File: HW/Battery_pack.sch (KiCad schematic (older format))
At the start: 10 parts

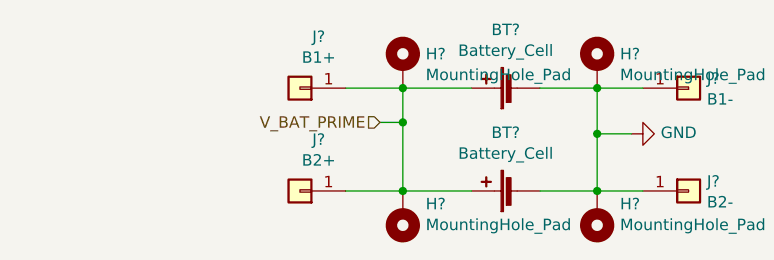
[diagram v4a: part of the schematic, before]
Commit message: add polyfuse for battery, remove resistor by SY8105, fix mistake by charger
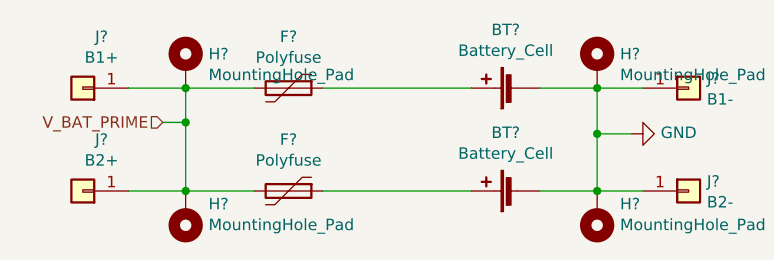
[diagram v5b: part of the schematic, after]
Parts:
- added F? (x2): Polyfuse, symbol Device:Polyfuse
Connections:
- net V_BAT_PRIME: now also F?.2, F?.2; no longer BT?.1 (+), BT?.1 (+)
- new net: BT?.1 (+), F?.1 (x2)
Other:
- moved on the sheet: H?, J?
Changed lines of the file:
@@
 $Descr A4 11693 8268
 encoding utf-8
-Sheet 8 42
+Sheet 13 42
 Title ""
 Date ""
@@
 L Connector_Generic:Conn_01x01 J?
 U 1 1 5F7477BC
-P 3950 3100
-F 0 "J?" H 3868 2875 50  0000 C CNN
-F 1 "B1+" H 3868 2966 50  0000 C CNN
-F 2 "" H 3950 3100 50  0001 C CNN
-F 3 "~" H 3950 3100 50  0001 C CNN
-	1    3950 3100
+P 3000 3100
+F 0 "J?" H 2918 2875 50  0000 C CNN
+F 1 "B1+" H 2918 2966 50  0000 C CNN
+F 2 "" H 3000 3100 50  0001 C CNN
+F 3 "~" H 3000 3100 50  0001 C CNN
+	1    3000 3100
 	-1   0    0    1
 $EndComp
@@
 L Connector_Generic:Conn_01x01 J?
 U 1 1 5F747F73
-P 3950 3550
-F 0 "J?" H 3868 3325 50  0000 C CNN
-F 1 "B2+" H 3868 3416 50  0000 C CNN
-F 2 "" H 3950 3550 50  0001 C CNN
-F 3 "~" H 3950 3550 50  0001 C CNN
-	1    3950 3550
+P 3000 3550
+F 0 "J?" H 2918 3325 50  0000 C CNN
+F 1 "B2+" H 2918 3416 50  0000 C CNN
+F 2 "" H 3000 3550 50  0001 C CNN
+F 3 "~" H 3000 3550 50  0001 C CNN
+	1    3000 3550
 	-1   0    0    1
 $EndComp
@@
 	5450 3100 5250 3100
 Wire Wire Line
-	4700 3100 4400 3100
+	3750 3100 3450 3100
 Wire Wire Line
-	4150 3550 4400 3550
+	3200 3550 3450 3550
 Wire Wire Line
 	5250 3100 5250 3300
@@
 	5250 3550 5000 3550
 Wire Wire Line
-	4400 3100 4400 3250
-Connection ~ 4400 3100
+	3450 3100 3450 3250
+Connection ~ 3450 3100
 Wire Wire Line
-	4400 3100 4150 3100
-Connection ~ 4400 3550
+	3450 3100 3200 3100
+Connection ~ 3450 3550
 Wire Wire Line
-	4400 3550 4700 3550
+	3450 3550 3750 3550
 $Comp
 L power:GND #PWR?
@@
 Wire Wire Line
 	5250 3300 5250 3550
-Text HLabel 4300 3250 0    50   Input ~ 0
+Text HLabel 3350 3250 0    50   Input ~ 0
 V_BAT_PRIME
 Wire Wire Line
-	4300 3250 4400 3250
-Connection ~ 4400 3250
+	3350 3250 3450 3250
+Connection ~ 3450 3250
 Wire Wire Line
-	4400 3250 4400 3550
+	3450 3250 3450 3550
 $Comp
 L Mechanical:MountingHole_Pad H?
 U 1 1 5F74F82F
-P 4400 3000
-F 0 "H?" H 4500 3049 50  0000 L CNN
-F 1 "MountingHole_Pad" H 4500 2958 50  0000 L CNN
-F 2 "" H 4400 3000 50  0001 C CNN
-F 3 "~" H 4400 3000 50  0001 C CNN
-	1    4400 3000
+P 3450 3000
+F 0 "H?" H 3550 3049 50  0000 L CNN
+F 1 "MountingHole_Pad" H 3550 2958 50  0000 L CNN
+F 2 "" H 3450 3000 50  0001 C CNN
+F 3 "~" H 3450 3000 50  0001 C CNN
+	1    3450 3000
 	1    0    0    -1
 $EndComp
@@
 L Mechanical:MountingHole_Pad H?
 U 1 1 5F7501BB
-P 4400 3650
-F 0 "H?" H 4300 3607 50  0000 R CNN
-F 1 "MountingHole_Pad" H 4300 3698 50  0000 R CNN
-F 2 "" H 4400 3650 50  0001 C CNN
-F 3 "~" H 4400 3650 50  0001 C CNN
-	1    4400 3650
+P 3450 3650
+F 0 "H?" H 3350 3607 50  0000 R CNN
+F 1 "MountingHole_Pad" H 3350 3698 50  0000 R CNN
+F 2 "" H 3450 3650 50  0001 C CNN
+F 3 "~" H 3450 3650 50  0001 C CNN
+	1    3450 3650
 	-1   0    0    1
 $EndComp
+$Comp
+L Device:Polyfuse F?
+U 1 1 5F77C417
+P 3900 3100
+F 0 "F?" V 3675 3100 50  0000 C CNN
+F 1 "Polyfuse" V 3766 3100 50  0000 C CNN
+F 2 "" H 3950 2900 50  0001 L CNN
+F 3 "~" H 3900 3100 50  0001 C CNN
+	1    3900 3100
+	0    1    1    0
+$EndComp
+$Comp
+L Device:Polyfuse F?
+U 1 1 5F77C5DC
+P 3900 3550
+F 0 "F?" V 3675 3550 50  0000 C CNN
+F 1 "Polyfuse" V 3766 3550 50  0000 C CNN
+F 2 "" H 3950 3350 50  0001 L CNN
+F 3 "~" H 3900 3550 50  0001 C CNN
+	1    3900 3550
+	0    1    1    0
+$EndComp
+Wire Wire Line
+	4050 3100 4700 3100
+Wire Wire Line
+	4050 3550 4700 3550
 $EndSCHEMATC

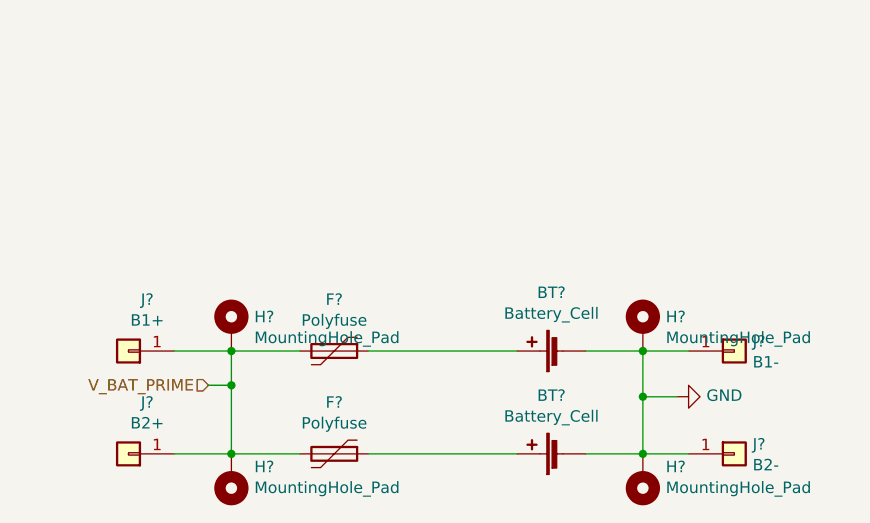
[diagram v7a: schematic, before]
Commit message: new battery pack schematic
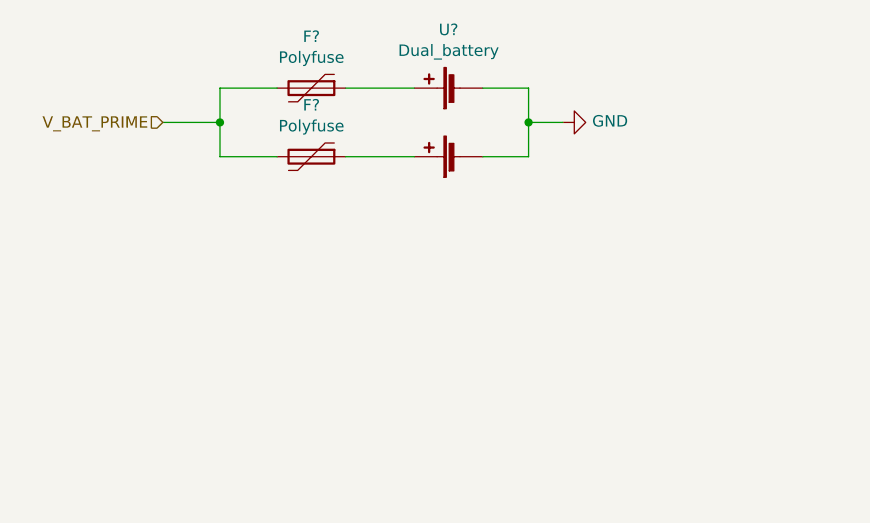
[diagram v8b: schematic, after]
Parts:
- removed BT? (x2): Battery_Cell, symbol Device:Battery_Cell
- removed H? (x4): MountingHole_Pad, symbol Mechanical:MountingHole_Pad
- removed J?: B1+, symbol Connector_Generic:Conn_01x01
- removed J?: B2+, symbol Connector_Generic:Conn_01x01
- removed J?: B1-, symbol Connector_Generic:Conn_01x01
- removed J?: B2-, symbol Connector_Generic:Conn_01x01
- added U?: Dual_battery, symbol symbols:Dual_battery
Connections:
- net GND: now also U?.~
- net at F?.1: now also U?.~ (x2)
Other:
- moved on the sheet: F?
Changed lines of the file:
@@
 $EndDescr
-$Comp
-L Device:Battery_Cell BT?
-U 1 1 5F746A46
-P 4900 3100
-F 0 "BT?" V 5155 3150 50  0000 C CNN
-F 1 "Battery_Cell" V 5064 3150 50  0000 C CNN
-F 2 "" V 4900 3160 50  0001 C CNN
-F 3 "~" V 4900 3160 50  0001 C CNN
-	1    4900 3100
-	0    -1   -1   0
-$EndComp
-$Comp
-L Device:Battery_Cell BT?
-U 1 1 5F7473CA
-P 4900 3550
-F 0 "BT?" V 5155 3600 50  0000 C CNN
-F 1 "Battery_Cell" V 5064 3600 50  0000 C CNN
-F 2 "" V 4900 3610 50  0001 C CNN
-F 3 "~" V 4900 3610 50  0001 C CNN
-	1    4900 3550
-	0    -1   -1   0
-$EndComp
-$Comp
-L Connector_Generic:Conn_01x01 J?
-U 1 1 5F7477BC
-P 3000 3100
-F 0 "J?" H 2918 2875 50  0000 C CNN
-F 1 "B1+" H 2918 2966 50  0000 C CNN
-F 2 "" H 3000 3100 50  0001 C CNN
-F 3 "~" H 3000 3100 50  0001 C CNN
-	1    3000 3100
-	-1   0    0    1
-$EndComp
-$Comp
-L Connector_Generic:Conn_01x01 J?
-U 1 1 5F747F73
-P 3000 3550
-F 0 "J?" H 2918 3325 50  0000 C CNN
-F 1 "B2+" H 2918 3416 50  0000 C CNN
-F 2 "" H 3000 3550 50  0001 C CNN
-F 3 "~" H 3000 3550 50  0001 C CNN
-	1    3000 3550
-	-1   0    0    1
-$EndComp
-$Comp
-L Connector_Generic:Conn_01x01 J?
-U 1 1 5F7482EC
-P 5650 3100
-F 0 "J?" H 5730 3142 50  0000 L CNN
-F 1 "B1-" H 5730 3051 50  0000 L CNN
-F 2 "" H 5650 3100 50  0001 C CNN
-F 3 "~" H 5650 3100 50  0001 C CNN
-	1    5650 3100
-	1    0    0    -1
-$EndComp
-$Comp
-L Connector_Generic:Conn_01x01 J?
-U 1 1 5F748B5C
-P 5650 3550
-F 0 "J?" H 5730 3592 50  0000 L CNN
-F 1 "B2-" H 5730 3501 50  0000 L CNN
-F 2 "" H 5650 3550 50  0001 C CNN
-F 3 "~" H 5650 3550 50  0001 C CNN
-	1    5650 3550
-	1    0    0    -1
-$EndComp
-Wire Wire Line
-	5450 3550 5250 3550
-Wire Wire Line
-	5450 3100 5250 3100
-Wire Wire Line
-	3750 3100 3450 3100
-Wire Wire Line
-	3200 3550 3450 3550
-Wire Wire Line
-	5250 3100 5250 3300
-Connection ~ 5250 3100
-Wire Wire Line
-	5250 3100 5000 3100
-Connection ~ 5250 3550
-Wire Wire Line
-	5250 3550 5000 3550
-Wire Wire Line
-	3450 3100 3450 3250
-Connection ~ 3450 3100
-Wire Wire Line
-	3450 3100 3200 3100
-Connection ~ 3450 3550
-Wire Wire Line
-	3450 3550 3750 3550
 $Comp
 L power:GND #PWR?
 U 1 1 5F74BC2B
-P 5400 3300
-F 0 "#PWR?" H 5400 3050 50  0001 C CNN
-F 1 "GND" V 5405 3172 50  0000 R CNN
-F 2 "" H 5400 3300 50  0001 C CNN
-F 3 "" H 5400 3300 50  0001 C CNN
-	1    5400 3300
+P 4900 2100
+F 0 "#PWR?" H 4900 1850 50  0001 C CNN
+F 1 "GND" V 4905 1972 50  0000 R CNN
+F 2 "" H 4900 2100 50  0001 C CNN
+F 3 "" H 4900 2100 50  0001 C CNN
+	1    4900 2100
 	0    -1   -1   0
 $EndComp
-Wire Wire Line
-	5400 3300 5250 3300
-Connection ~ 5250 3300
-Wire Wire Line
-	5250 3300 5250 3550
-Text HLabel 3350 3250 0    50   Input ~ 0
+Text HLabel 3150 2100 0    50   Input ~ 0
 V_BAT_PRIME
-Wire Wire Line
-	3350 3250 3450 3250
-Connection ~ 3450 3250
-Wire Wire Line
-	3450 3250 3450 3550
-$Comp
-L Mechanical:MountingHole_Pad H?
-U 1 1 5F74F82F
-P 3450 3000
-F 0 "H?" H 3550 3049 50  0000 L CNN
-F 1 "MountingHole_Pad" H 3550 2958 50  0000 L CNN
-F 2 "" H 3450 3000 50  0001 C CNN
-F 3 "~" H 3450 3000 50  0001 C CNN
-	1    3450 3000
-	1    0    0    -1
-$EndComp
-$Comp
-L Mechanical:MountingHole_Pad H?
-U 1 1 5F74FBB0
-P 5250 3000
-F 0 "H?" H 5350 3049 50  0000 L CNN
-F 1 "MountingHole_Pad" H 5350 2958 50  0000 L CNN
-F 2 "" H 5250 3000 50  0001 C CNN
-F 3 "~" H 5250 3000 50  0001 C CNN
-	1    5250 3000
-	1    0    0    -1
-$EndComp
-$Comp
-L Mechanical:MountingHole_Pad H?
-U 1 1 5F74FE56
-P 5250 3650
-F 0 "H?" H 5150 3607 50  0000 R CNN
-F 1 "MountingHole_Pad" H 5150 3698 50  0000 R CNN
-F 2 "" H 5250 3650 50  0001 C CNN
-F 3 "~" H 5250 3650 50  0001 C CNN
-	1    5250 3650
-	-1   0    0    1
-$EndComp
-$Comp
-L Mechanical:MountingHole_Pad H?
-U 1 1 5F7501BB
-P 3450 3650
-F 0 "H?" H 3350 3607 50  0000 R CNN
-F 1 "MountingHole_Pad" H 3350 3698 50  0000 R CNN
-F 2 "" H 3450 3650 50  0001 C CNN
-F 3 "~" H 3450 3650 50  0001 C CNN
-	1    3450 3650
-	-1   0    0    1
-$EndComp
 $Comp
 L Device:Polyfuse F?
 U 1 1 5F77C417
-P 3900 3100
-F 0 "F?" V 3675 3100 50  0000 C CNN
-F 1 "Polyfuse" V 3766 3100 50  0000 C CNN
-F 2 "" H 3950 2900 50  0001 L CNN
-F 3 "~" H 3900 3100 50  0001 C CNN
-	1    3900 3100
+P 3800 1950
+F 0 "F?" V 3575 1950 50  0000 C CNN
+F 1 "Polyfuse" V 3666 1950 50  0000 C CNN
+F 2 "" H 3850 1750 50  0001 L CNN
+F 3 "~" H 3800 1950 50  0001 C CNN
+	1    3800 1950
 	0    1    1    0
 $EndComp
@@
 L Device:Polyfuse F?
 U 1 1 5F77C5DC
-P 3900 3550
-F 0 "F?" V 3675 3550 50  0000 C CNN
-F 1 "Polyfuse" V 3766 3550 50  0000 C CNN
-F 2 "" H 3950 3350 50  0001 L CNN
-F 3 "~" H 3900 3550 50  0001 C CNN
-	1    3900 3550
+P 3800 2250
+F 0 "F?" V 3575 2250 50  0000 C CNN
+F 1 "Polyfuse" V 3666 2250 50  0000 C CNN
+F 2 "" H 3850 2050 50  0001 L CNN
+F 3 "~" H 3800 2250 50  0001 C CNN
+	1    3800 2250
 	0    1    1    0
 $EndComp
+$Comp
+L symbols:Dual_battery U?
+U 1 1 5F8A8975
+P 4400 2100
+F 0 "U?" H 4400 2505 50  0000 C CNN
+F 1 "Dual_battery" H 4400 2414 50  0000 C CNN
+F 2 "" H 4400 2100 50  0001 C CNN
+F 3 "" H 4400 2100 50  0001 C CNN
+	1    4400 2100
+	1    0    0    -1
+$EndComp
 Wire Wire Line
-	4050 3100 4700 3100
+	3650 1950 3400 1950
 Wire Wire Line
-	4050 3550 4700 3550
+	3400 1950 3400 2100
+Wire Wire Line
+	3400 2250 3650 2250
+Wire Wire Line
+	3150 2100 3400 2100
+Connection ~ 3400 2100
+Wire Wire Line
+	3400 2100 3400 2250
+Wire Wire Line
+	4550 1950 4750 1950
+Wire Wire Line
+	4750 1950 4750 2100
+Wire Wire Line
+	4750 2250 4550 2250
+Connection ~ 4750 2100
+Wire Wire Line
+	4750 2100 4750 2250
+Wire Wire Line
+	4750 2100 4900 2100
+Wire Wire Line
+	3950 1950 4250 1950
+Wire Wire Line
+	4250 2250 3950 2250
 $EndSCHEMATC
